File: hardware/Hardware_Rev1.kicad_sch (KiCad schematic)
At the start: 150 parts, among them J1 RJ45_LED_Shielded, Q1 BSS138, Q10 Q_PMOS_GSD, Q11 Q_PMOS_GSD, Q12 Q_PMOS_GSD, Q13 BSS138, Q14 BSS138, Q15 BSS138, Q16 Q_PMOS_GSD, Q17 Q_PMOS_GSD, Q18 Q_PMOS_GSD, Q19 BSS138, Q2 BSS138, Q20 BSS138, Q21 BSS138, Q22 Q_PMOS_GSD, Q23 Q_PMOS_GSD, Q24 Q_PMOS_GSD, Q3 BSS138, Q4 Q_PMOS_GSD, Q5 Q_PMOS_GSD, Q6 Q_PMOS_GSD, Q7 BSS138, Q8 BSS138, Q9 BSS138, U1 OKI, U2 Teensy4.1_DEV-16771

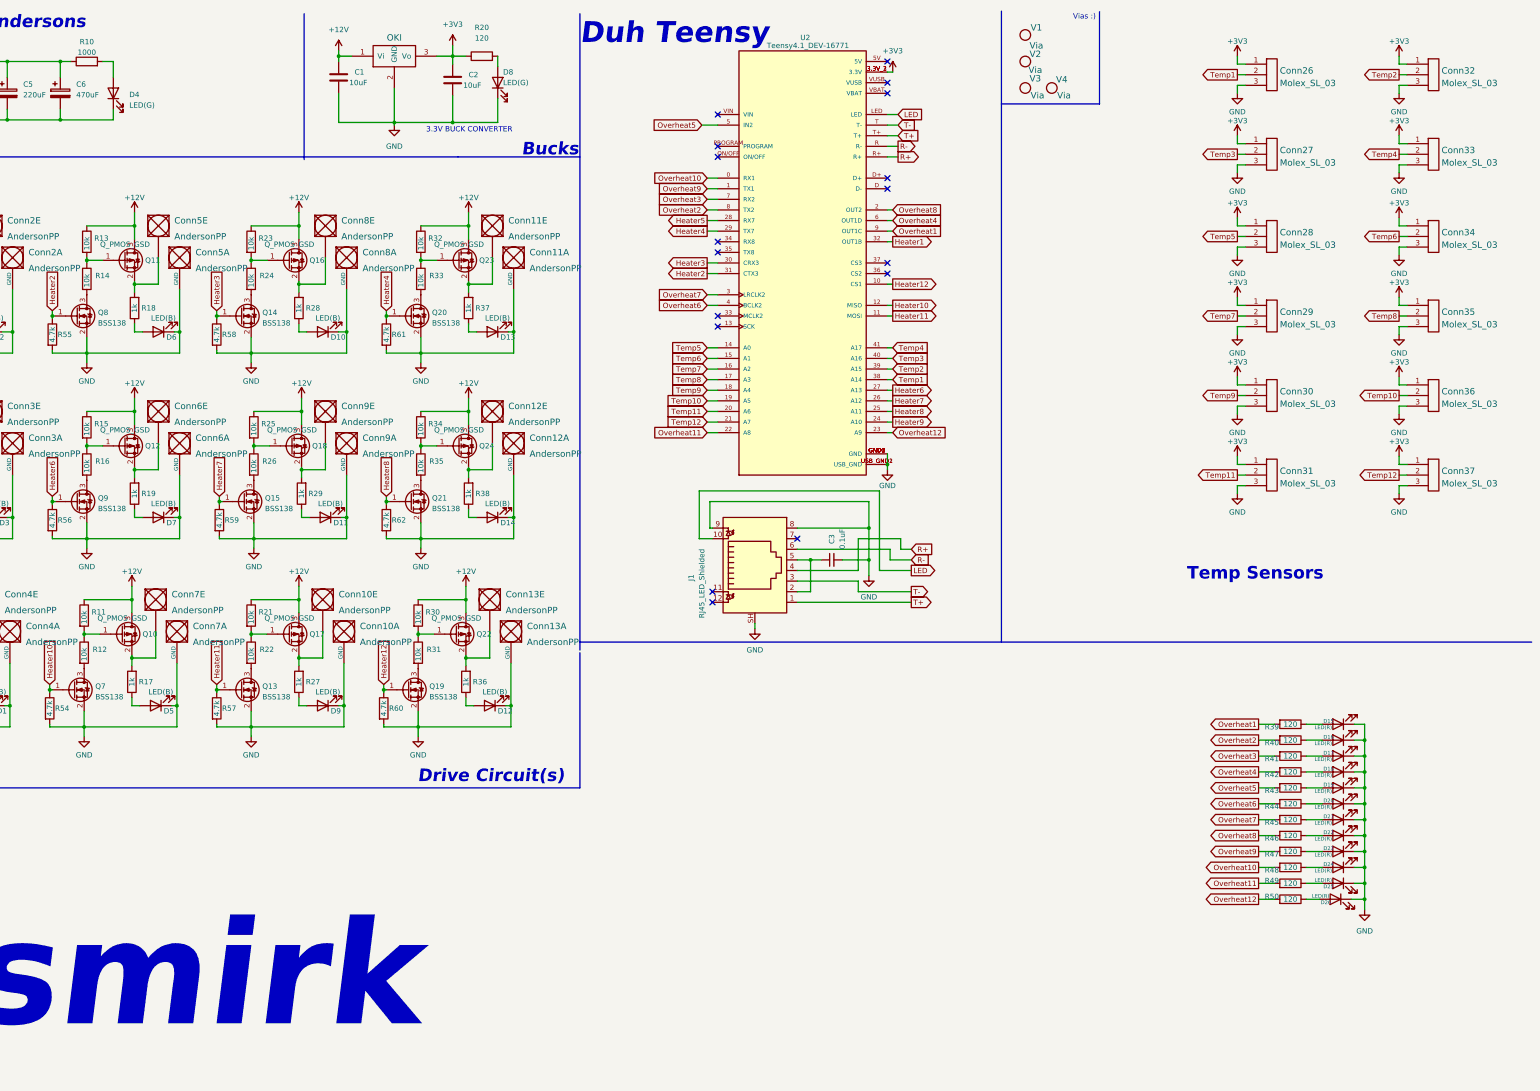
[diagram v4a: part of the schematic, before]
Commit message: Cleaned up schematic
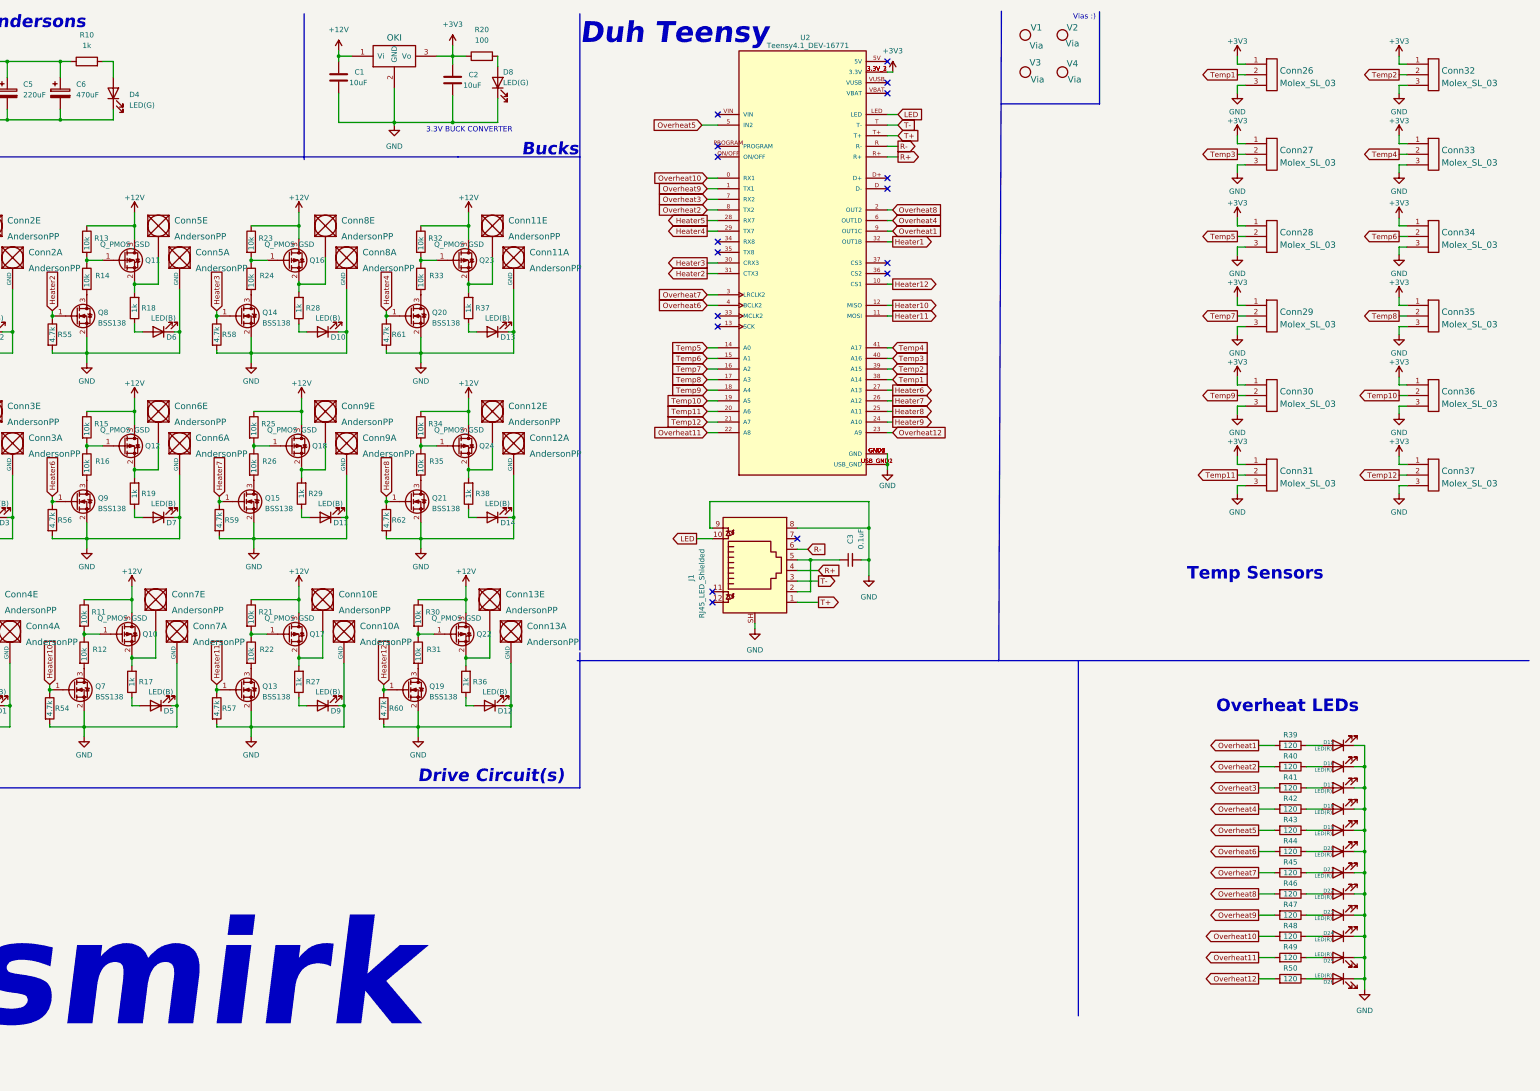
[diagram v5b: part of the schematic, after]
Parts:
- R10: value 1000 -> 1k
- R20: value 120 -> 100
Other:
- note added: "Overheat LEDs"
- moved on the sheet: C3, D15, D16, D17, D18, D19, D20, D21, D22, D23, D24, D25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

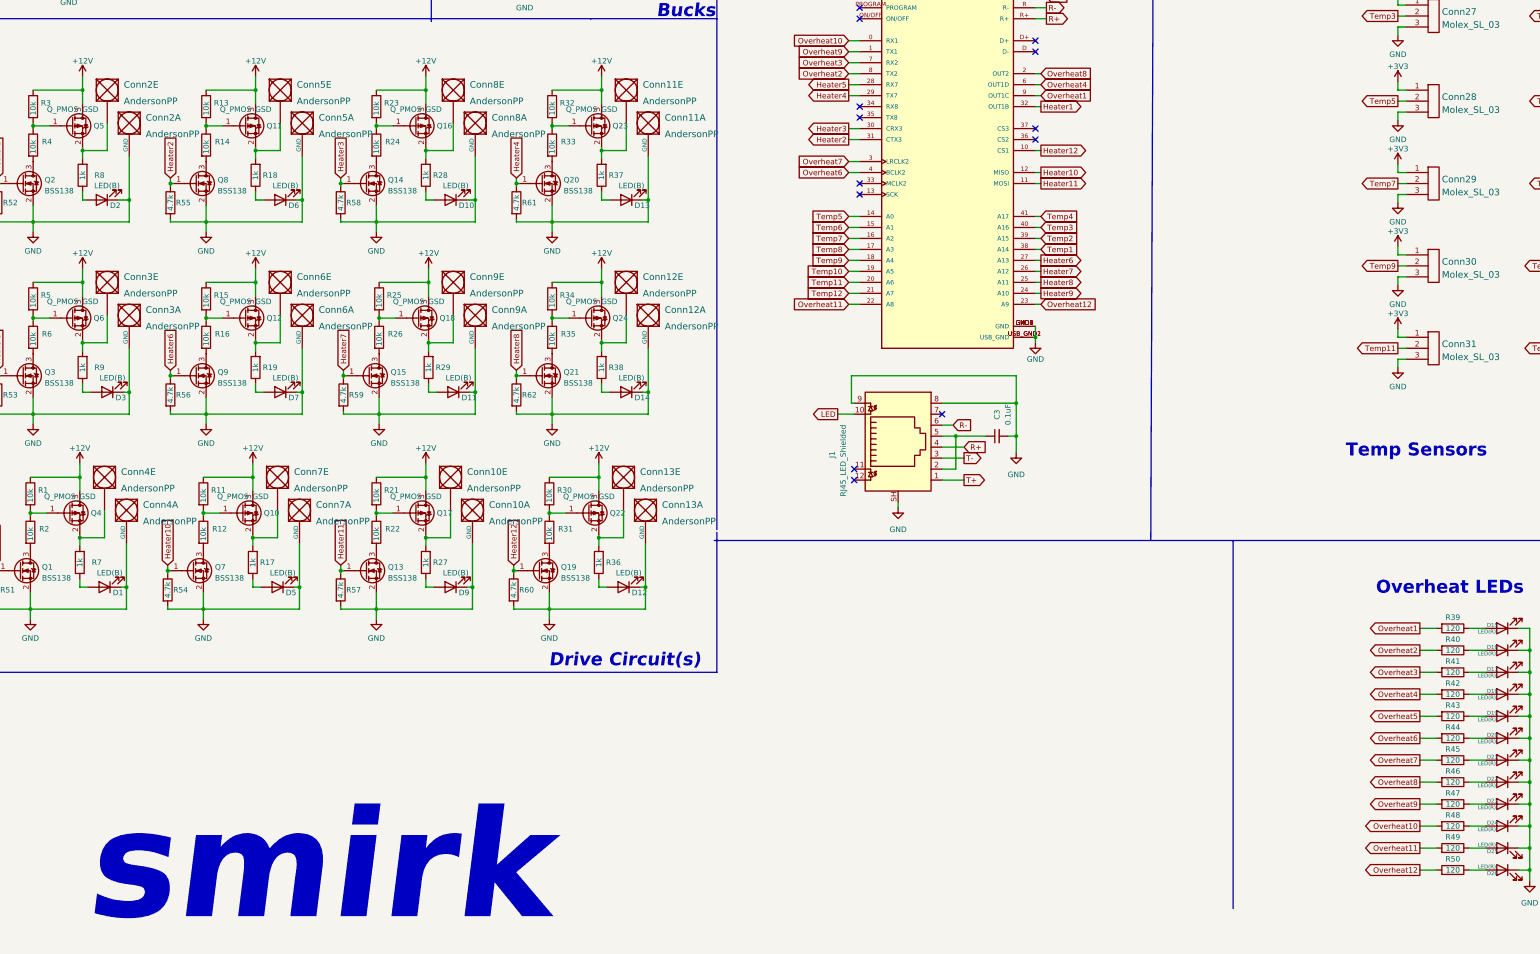
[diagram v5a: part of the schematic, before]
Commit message: Started layout heater ports
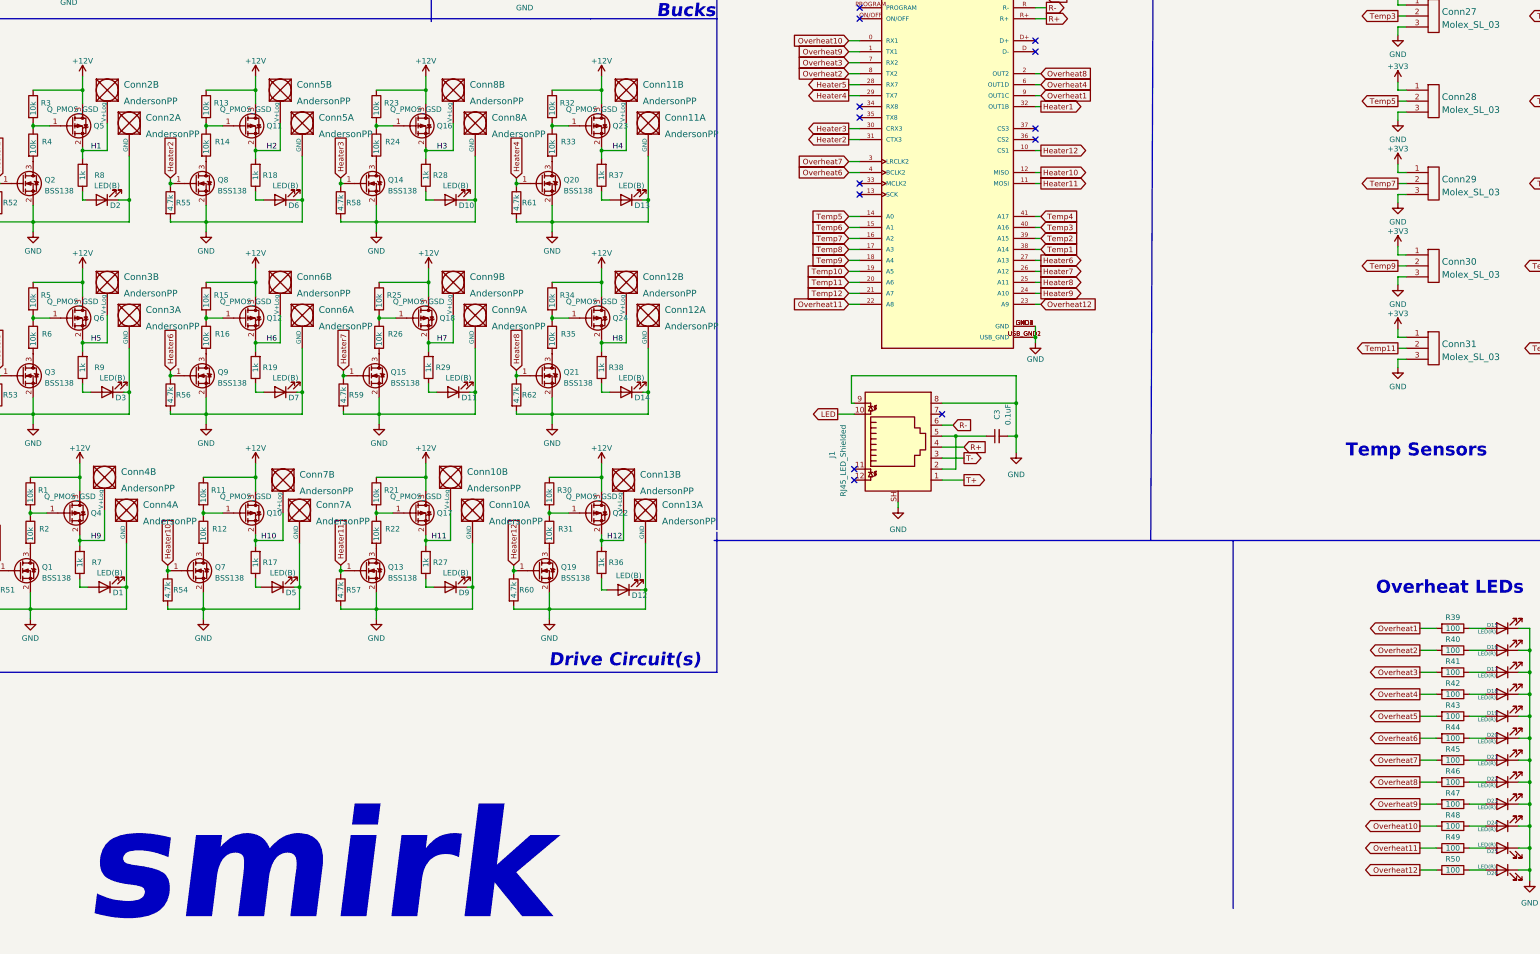
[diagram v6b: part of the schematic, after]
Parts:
- R39, R40, R41, R42, R43, R44, R45, R46, R47, R48, R49, R50: value 120 -> 100
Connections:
- net H2: now reaches Q11.2 (S), R18.2
- net H2: now also Conn5.2 (V+Log); no longer Conn5.1
- net H3: now reaches Q16.2 (S), R28.2
- net H3: now also Conn8.2 (V+Log); no longer Conn8.1
- net H4: now reaches Q23.2 (S), R37.2
- net H4: now also Conn11.2 (V+Log); no longer Conn11.1
- net H10: now reaches Q10.2 (S), R17.2
- net H10: now also Conn7.2 (V+Log); no longer Conn7.1
- net H11: now reaches Q17.2 (S), R27.2
- net H11: now also Conn10.2 (V+Log); no longer Conn10.1
- net H5: now reaches Q6.2 (S), R9.2
- net H5: now also Conn3.2 (V+Log); no longer Conn3.1
- net H6: now reaches Q12.2 (S), R19.2
- net H6: now also Conn6.2 (V+Log); no longer Conn6.1
- net H1: now reaches Q5.2 (S), R8.2
- net H1: now also Conn2.2 (V+Log); no longer Conn2.1
- net H9: now reaches Q4.2 (S), R7.2
- net H9: now also Conn4.2 (V+Log); no longer Conn4.1
- net H12: now reaches Q22.2 (S), R36.2
- net H12: now also Conn13.2 (V+Log); no longer Conn13.1
- net H8: now reaches Q24.2 (S), R38.2
- net H8: now also Conn12.2 (V+Log); no longer Conn12.1
- net H7: now reaches Q18.2 (S), R29.2
- net H7: now also Conn9.2 (V+Log); no longer Conn9.1
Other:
- company: Jacob Byers, Joshua Perkins -> Grant Brinker
- title: Water Heater Board - Rev2? -> Heater Board - Rev2
- moved on the sheet: D12, Q10, Q22, R17, R36

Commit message: Finished components + Traces
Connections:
- net Overheat1: now also U2.23 (A9); no longer U2.9 (OUT1C)
- net Overheat10: now also U2.2 (OUT2); no longer U2.0 (RX1)
- net Overheat11: now also U2.1 (TX1); no longer U2.22 (A8)
- net Overheat12: now also U2.0 (RX1); no longer U2.23 (A9)
- net Overheat2: now also U2.22 (A8); no longer U2.8 (TX2)
- net Overheat3: now also U2.9 (OUT1C); no longer U2.7 (RX2)
- net Overheat4: now also U2.8 (TX2); no longer U2.6 (OUT1D)
- net Overheat5: now also U2.7 (RX2); no longer U2.5 (IN2)
- net Overheat6: now also U2.6 (OUT1D); no longer U2.4 (BCLK2)
- net Overheat7: now also U2.5 (IN2); no longer U2.3 (LRCLK2)
- net Overheat8: now also U2.4 (BCLK2); no longer U2.2 (OUT2)
- net Overheat9: now also U2.3 (LRCLK2); no longer U2.1 (TX1)
